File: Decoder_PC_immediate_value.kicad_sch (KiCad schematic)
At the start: 27 parts, among them Q1 BC818

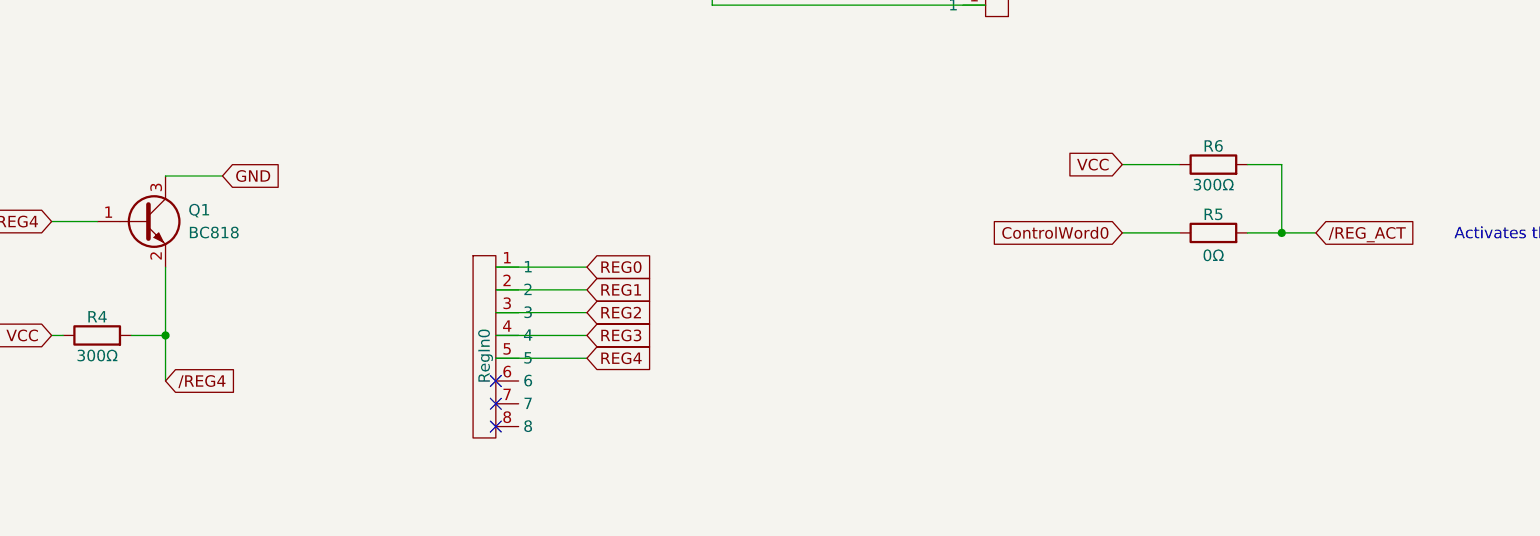
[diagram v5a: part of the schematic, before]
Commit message: Added Test Points
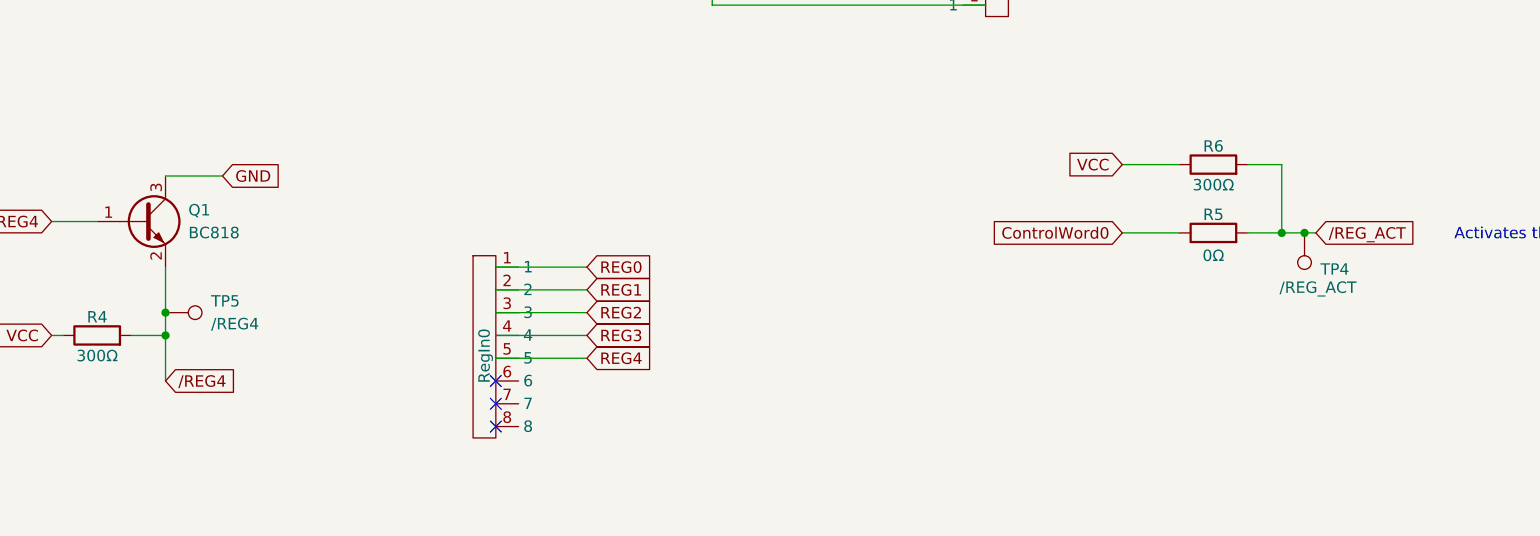
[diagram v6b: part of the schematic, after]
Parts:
- added TP4: /REG_ACT, TestPoint:TestPoint_Pad_D1.0mm, symbol Connector:TestPoint
- added TP5: /REG4, TestPoint:TestPoint_Pad_D1.0mm, symbol Connector:TestPoint
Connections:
- net /REG4: now also TP5.1
- net /REG_ACT: now also TP4.1
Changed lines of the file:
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@@
 	)
 	(junction
+		(at 214.63 157.48)
+		(diameter 0)
+		(color 0 0 0 0)
+	)
+	(junction
 		(at 157.48 59.69)
 		(diameter 0)
@@
 	)
 	(junction
+		(at 87.63 166.37)
+		(diameter 0)
+		(color 0 0 0 0)
+	)
+	(junction
 		(at 212.09 157.48)
 		(diameter 0)
@@
 	(wire
 		(pts
+			(xy 214.63 157.48) (xy 215.9 157.48)
+		)
+		(stroke
+			(width 0)
+			(type default)
+		)
+	)
+	(wire
+		(pts
 			(xy 22.86 99.06) (xy 39.37 99.06)
 		)
@@
 	(wire
 		(pts
-			(xy 87.63 161.29) (xy 87.63 168.91)
+			(xy 87.63 161.29) (xy 87.63 166.37)
 		)
 		(stroke
@@
 	(wire
 		(pts
-			(xy 212.09 157.48) (xy 215.9 157.48)
+			(xy 212.09 157.48) (xy 214.63 157.48)
 		)
 		(stroke
@@
 	(wire
 		(pts
+			(xy 87.63 166.37) (xy 87.63 168.91)
+		)
+		(stroke
+			(width 0)
+			(type default)
+		)
+	)
+	(wire
+		(pts
 			(xy 62.23 41.91) (xy 71.12 41.91)
 		)
@@
 	)
 	(symbol
+		(lib_id "Connector:TestPoint")
+		(at 87.63 166.37 270)
+		(unit 1)
+		(exclude_from_sim no)
+		(in_bom yes)
+		(on_board yes)
+		(dnp no)
+		(fields_autoplaced yes)
+		(property "Reference" "TP5"
+			(at 92.71 165.0999 90)
+			(effects
+				(font
+					(size 1.27 1.27)
+				)
+				(justify left)
+			)
+		)
+		(property "Value" "/REG4"
+			(at 92.71 167.6399 90)
+			(effects
+				(font
+					(size 1.27 1.27)
+				)
+				(justify left)
+			)
+		)
+		(property "Footprint" "TestPoint:TestPoint_Pad_D1.0mm"
+			(at 87.63 171.45 0)
+			(effects
+				(font
+					(size 1.27 1.27)
+				)
+				(hide yes)
+			)
+		)
+		(property "Datasheet" "~"
+			(at 87.63 171.45 0)
+			(effects
+				(font
+					(size 1.27 1.27)
+				)
+				(hide yes)
+			)
+		)
+		(property "Description" "test point"
+			(at 87.63 166.37 0)
+			(effects
+				(font
+					(size 1.27 1.27)
+				)
+				(hide yes)
+			)
+		)
+		(pin "1"
+		)
+		(instances
+			(project ""
+				(path "/98f98096-bf3a-4810-aa49-8450648e3ec5"
+					(reference "TP5")
+					(unit 1)
+				)
+			)
+		)
+	)
+	(symbol
 		(lib_id "Device:C_Small")
 		(at 170.18 93.98 0)
@@
 					(unit 1)
 				)
+			)
+		)
+	)
+	(symbol
+		(lib_id "Connector:TestPoint")
+		(at 214.63 157.48 180)
+		(unit 1)
+		(exclude_from_sim no)
+		(in_bom yes)
+		(on_board yes)
+		(dnp no)
+		(property "Reference" "TP4"
+			(at 216.408 161.544 0)
+			(effects
+				(font
+					(size 1.27 1.27)
+				)
+				(justify right)
+			)
+		)
+		(property "Value" "/REG_ACT"
+			(at 211.836 163.576 0)
+			(effects
+				(font
+					(size 1.27 1.27)
+				)
+				(justify right)
+			)
+		)
+		(property "Footprint" "TestPoint:TestPoint_Pad_D1.0mm"
+			(at 209.55 157.48 0)
+			(effects
+				(font
+					(size 1.27 1.27)
+				)
+				(hide yes)
+			)
+		)
+		(property "Datasheet" "~"
+			(at 209.55 157.48 0)
+			(effects
+				(font
+					(size 1.27 1.27)
+				)
+				(hide yes)
+			)
+		)
+		(property "Description" "test point"
+			(at 214.63 157.48 0)
+			(effects
+				(font
+					(size 1.27 1.27)
+				)
+				(hide yes)
+			)
+		)
+		(pin "1"
+		)
+		(instances
+			(project ""
+				(path "/98f98096-bf3a-4810-aa49-8450648e3ec5"
+					(reference "TP4")
+					(unit 1)
+				)

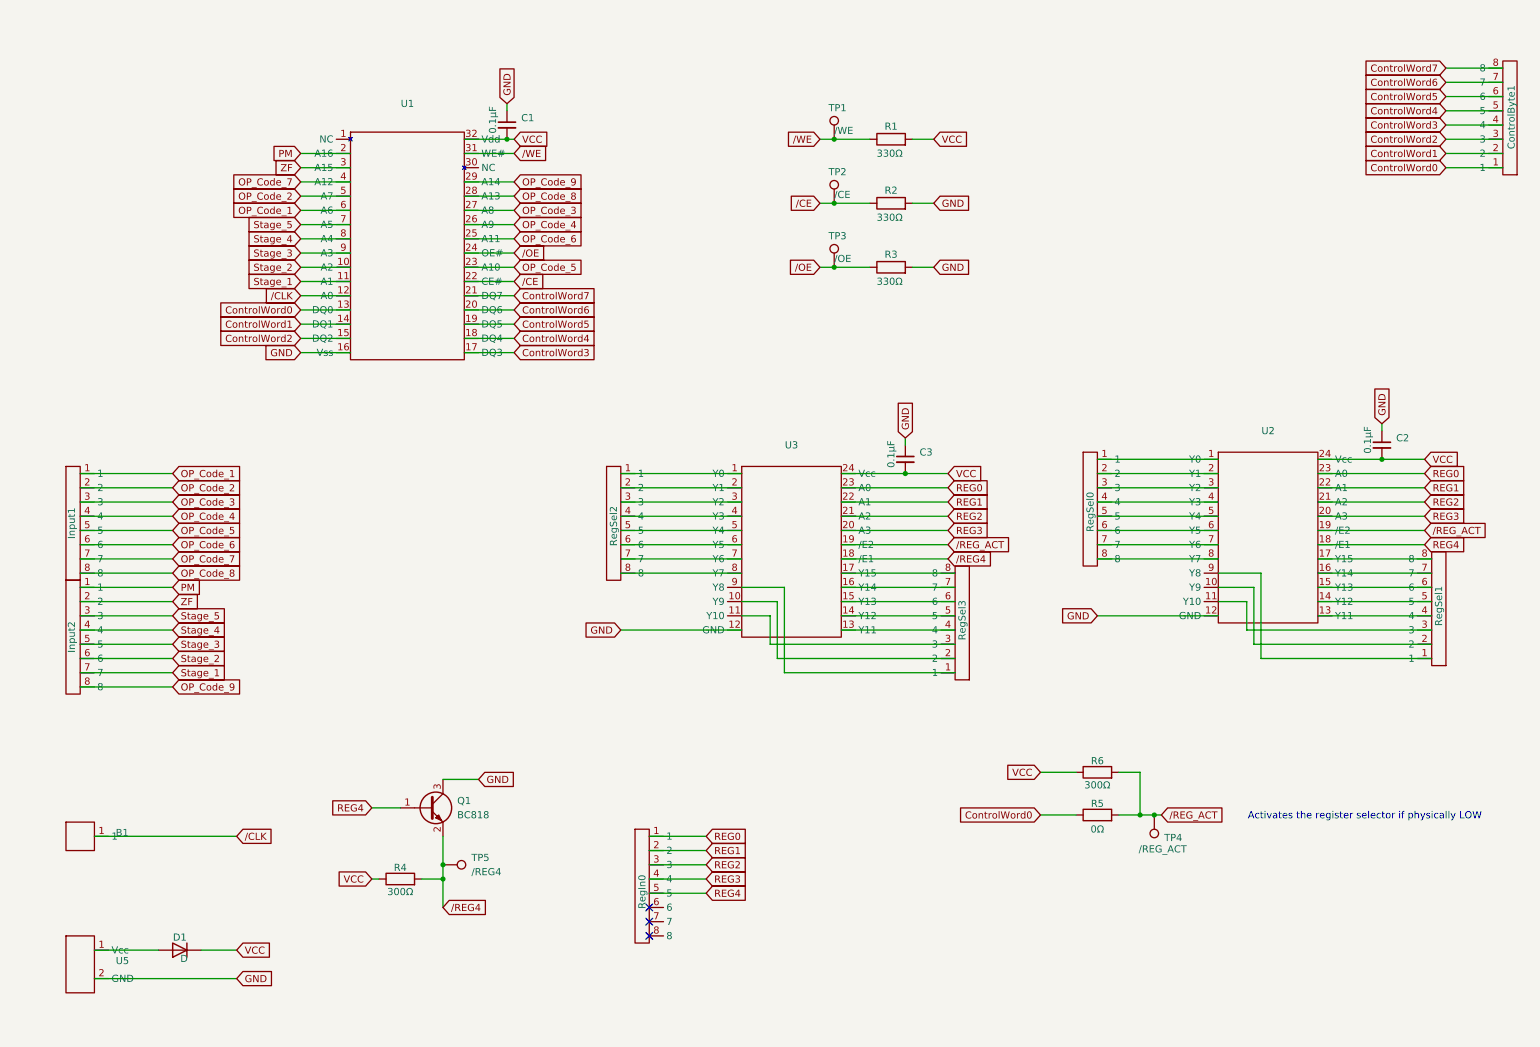
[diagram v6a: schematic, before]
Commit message: Added Bulk Capacitor
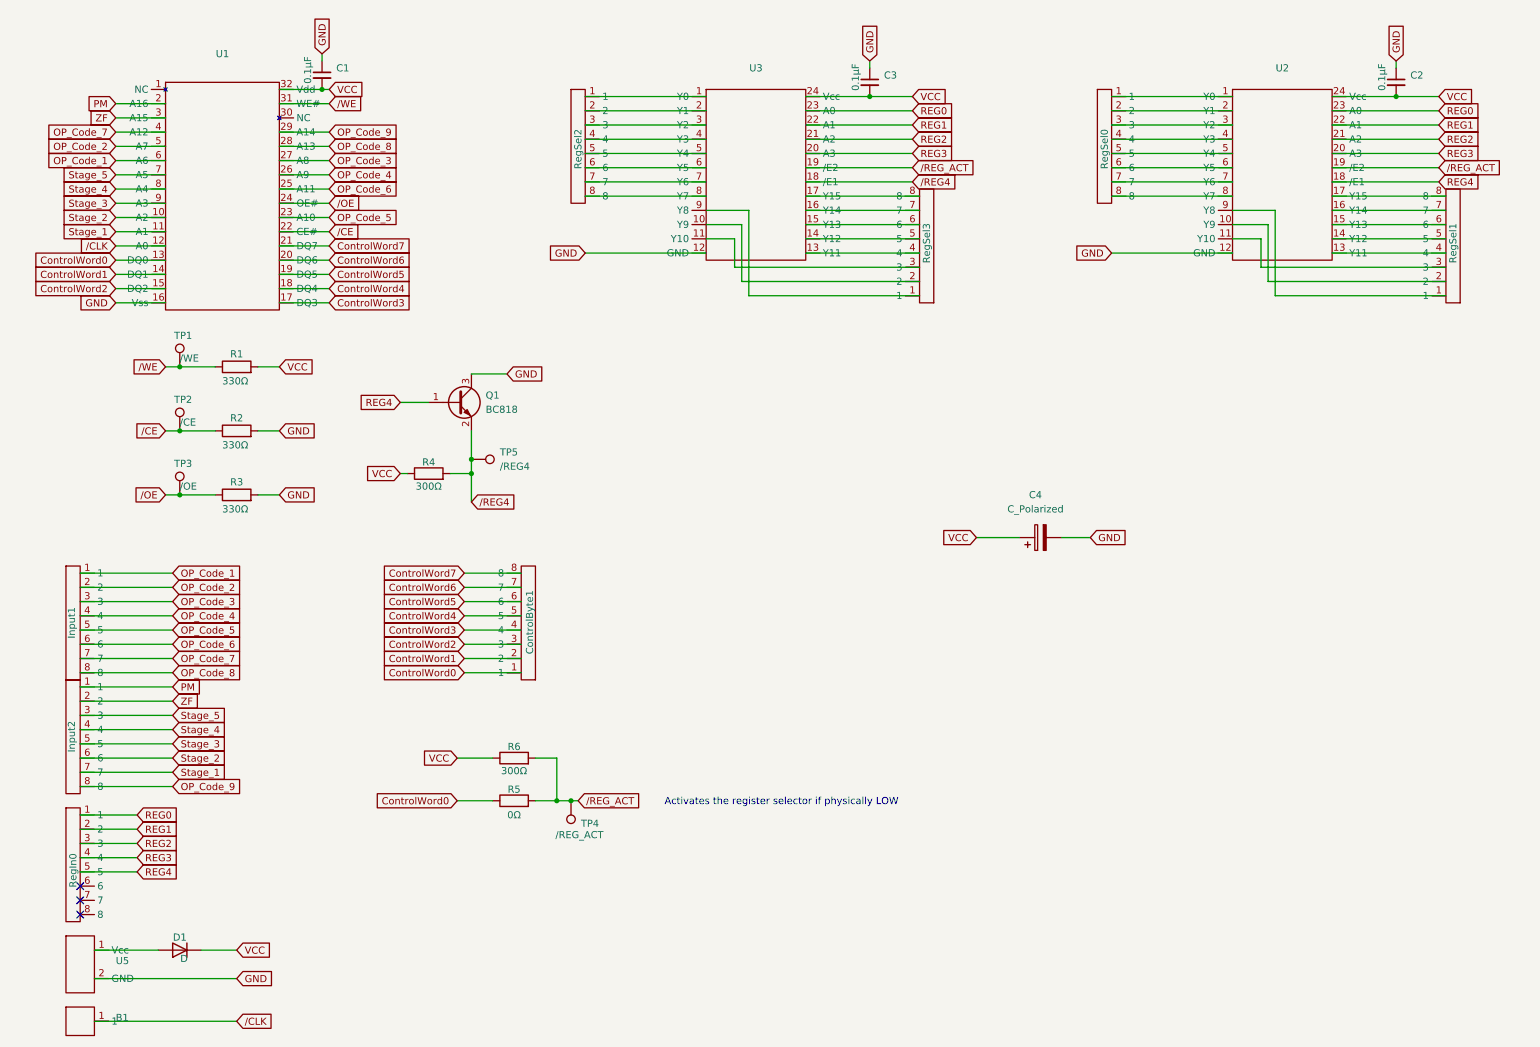
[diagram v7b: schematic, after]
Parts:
- added C4: C_Polarized, Capacitor_THT:CP_Radial_D6.3mm_P2.50mm, symbol Device:C_Polarized
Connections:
- net GND: now also C4.2
- net VCC: now also C4.1
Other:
- moved on the sheet: B1, C1, C2, C3, ControlByte1, Input1, Input2, Q1, R1, R2, R3, R4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

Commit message: Corrected Position of Diode
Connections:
- net GND: now also D1.2 (A); no longer U5.2 (GND)
- net VCC: now also U5.1 (Vcc); no longer D1.1 (K)
- new net: D1.1 (K), U5.2 (GND)
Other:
- moved on the sheet: D1
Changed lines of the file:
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@@
 	(wire
 		(pts
+			(xy 44.45 186.69) (xy 50.8 186.69)
+		)
+		(stroke
+			(width 0)
+			(type default)
+		)
+	)
+	(wire
+		(pts
 			(xy 29.21 35.56) (xy 38.1 35.56)
 		)
@@
 	(wire
 		(pts
-			(xy 25.4 181.61) (xy 36.83 181.61)
-		)
-		(stroke
-			(width 0)
-			(type default)
-		)
-	)
-	(wire
-		(pts
 			(xy 246.38 34.29) (xy 265.43 34.29)
 		)
@@
 	(wire
 		(pts
-			(xy 25.4 186.69) (xy 50.8 186.69)
-		)
-		(stroke
-			(width 0)
-			(type default)
-		)
-	)
-	(wire
-		(pts
 			(xy 58.42 40.64) (xy 67.31 40.64)
 		)
@@
 	(wire
 		(pts
+			(xy 25.4 186.69) (xy 36.83 186.69)
+		)
+		(stroke
+			(width 0)
+			(type default)
+		)
+	)
+	(wire
+		(pts
 			(xy 22.86 119.38) (xy 39.37 119.38)
 		)
@@
 	(wire
 		(pts
-			(xy 54.61 88.9) (xy 58.42 88.9)
+			(xy 25.4 181.61) (xy 50.8 181.61)
 		)
 		(stroke
@@
 	(wire
 		(pts
-			(xy 163.83 22.86) (xy 163.83 24.13)
+			(xy 54.61 88.9) (xy 58.42 88.9)
 		)
 		(stroke
@@
 	(wire
 		(pts
-			(xy 44.45 181.61) (xy 50.8 181.61)
+			(xy 163.83 22.86) (xy 163.83 24.13)
 		)
 		(stroke
@@
 	(symbol
 		(lib_id "Device:D")
-		(at 40.64 181.61 180)
+		(at 40.64 186.69 0)
 		(unit 1)
 		(exclude_from_sim no)
@@
 		(dnp no)
 		(property "Reference" "D1"
-			(at 40.64 179.324 0)
+			(at 40.64 188.976 0)
 			(effects
 				(font
@@
 		)
 		(property "Value" "D"
-			(at 41.402 183.134 0)
+			(at 39.878 185.166 0)
 			(effects
 				(font
@@
 		)
 		(property "Footprint" "Diode_THT:D_5W_P10.16mm_Horizontal"
-			(at 40.64 181.61 0)
+			(at 40.64 186.69 0)
 			(effects
 				(font
@@
 		)
 		(property "Datasheet" "~"
-			(at 40.64 181.61 0)
+			(at 40.64 186.69 0)
 			(effects
 				(font
@@
 		)
 		(property "Description" "Diode"
-			(at 40.64 181.61 0)
+			(at 40.64 186.69 0)
 			(effects
 				(font
@@
 		)
 		(property "Sim.Device" "D"
-			(at 40.64 181.61 0)
+			(at 40.64 186.69 0)
 			(effects
 				(font
@@
 		)
 		(property "Sim.Pins" "1=K 2=A"
-			(at 40.64 181.61 0)
+			(at 40.64 186.69 0)
 			(effects
 				(font
